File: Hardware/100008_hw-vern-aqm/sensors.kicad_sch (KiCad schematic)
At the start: 5 parts

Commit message: schematic work
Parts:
- removed C?: 10u, Capacitor_SMD:C_0805_2012Metric, symbol Device:C
- removed C?: 1u, Capacitor_SMD:C_0805_2012Metric, symbol Device:C
- removed C?: 100n, Capacitor_SMD:C_0603_1608Metric, symbol Device:C
- removed R?: 10k, Resistor_SMD:R_0603_1608Metric, symbol Device:R
- added C? (x3): 100n, Capacitor_SMD:C_0603_1608Metric, symbol Device:C
- added R? (x3): 10k, Resistor_SMD:R_0603_1608Metric, symbol Device:R
- added U?: DPS368, Components:LGA8S145X65P2X4_200X250X110-V, symbol ICs:DPS368
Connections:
- net +3V3: now also U?.19 (VDD), U?.7 (VDD), C?.1, C?.1, C?.1, R?.1, R?.1, U?.6 (VDDIO), U?.8 (VDD)
- net GND: now also U?.20 (GND), U?.21 (GND), U?.6 (GND), C?.2, C?.2, C?.2, R?.2, U?.1 (GND), U?.7 (GND)
- net I2C_SCL: now also U?.9 (SCL), R?.2, U?.4 (SCK)
- net I2C_SDA: now also U?.10 (SDA), R?.2, U?.3 (SDI)
- new net: R?.1, U?.5 (SDO)
- no-connect marks 0 -> 1
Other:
- note added: "Infineon DPS368 barometric pressure sensor"
- note added: "Sensirion SCD40 CO2 sensor"
- moved on the sheet: U?

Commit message: schematic work
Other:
- note added: "Design-in Guide SCD4x CO2 Sensor"
- note removed: "Flexible I/O worked examples"
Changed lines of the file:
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@@
 		)
 	)
-	(text_box "LAYOUT NOTE:\nEnsure good coupling to ambinet air, shield from direct sunlight and decouple from external heat sources"
+	(text_box "LAYOUT NOTE:\nEnsure good coupling to ambinet air, decouple from external heat sources, shield from direct sunlight and air turbulences"
 		(exclude_from_sim no)
-		(at 214.63 148.59 0)
-		(size 39.37 11.43)
+		(at 213.36 148.59 0)
+		(size 40.64 12.7)
 		(stroke
 			(width 0.8)
@@
 	(text_box "DESIGN NOTE:\nI2C address is 0x77 or 0x76 if SDO pin is pulled low."
 		(exclude_from_sim no)
-		(at 240.03 82.55 0)
-		(size 22.86 11.43)
+		(at 237.49 85.09 0)
+		(size 25.4 8.89)
 		(stroke
 			(width 0.8)
@@
 		)
 	)
-	(text "Flexible I/O worked examples"
+	(text "Design-in Guide SCD4x CO2 Sensor"
 		(exclude_from_sim no)
 		(at 265.43 254 0)
@@
 			)
 			(justify left bottom)
-			(href "https://jpieper.com/2022/06/30/flexible-i-o-worked-examples/")
+			(href "https://sensirion.com/media/documents/0D0C9129/623B1183/Sensirion_CO2_Sensors_SCD4x_design-in_guide.pdf")
 		)
 	)

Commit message: schematic and pcb layout
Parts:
- added C19: 100n, Capacitor_SMD:C_0603_1608Metric, symbol Device:C
- gave numbers to parts that had none: 8
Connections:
- net +3V3: now also C19.1
- net GND: now also C19.2
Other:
- moved on the sheet: C16, C17, C18, R32, R33, R34, U4, U5

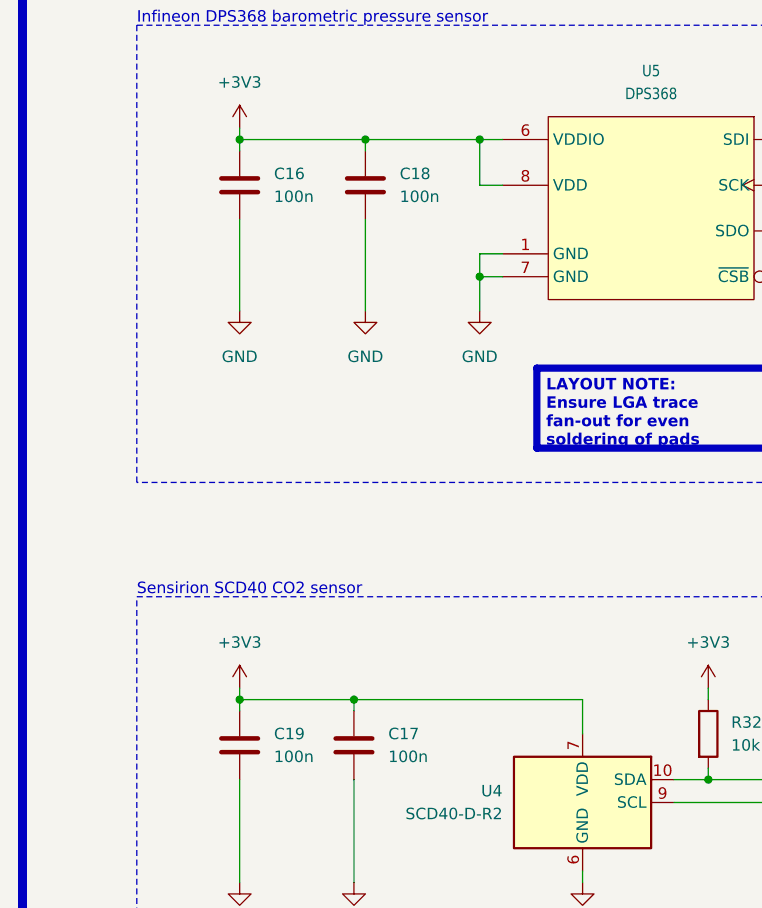
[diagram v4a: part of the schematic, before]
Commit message: schematic, pcb layout, added mouser shoping cart
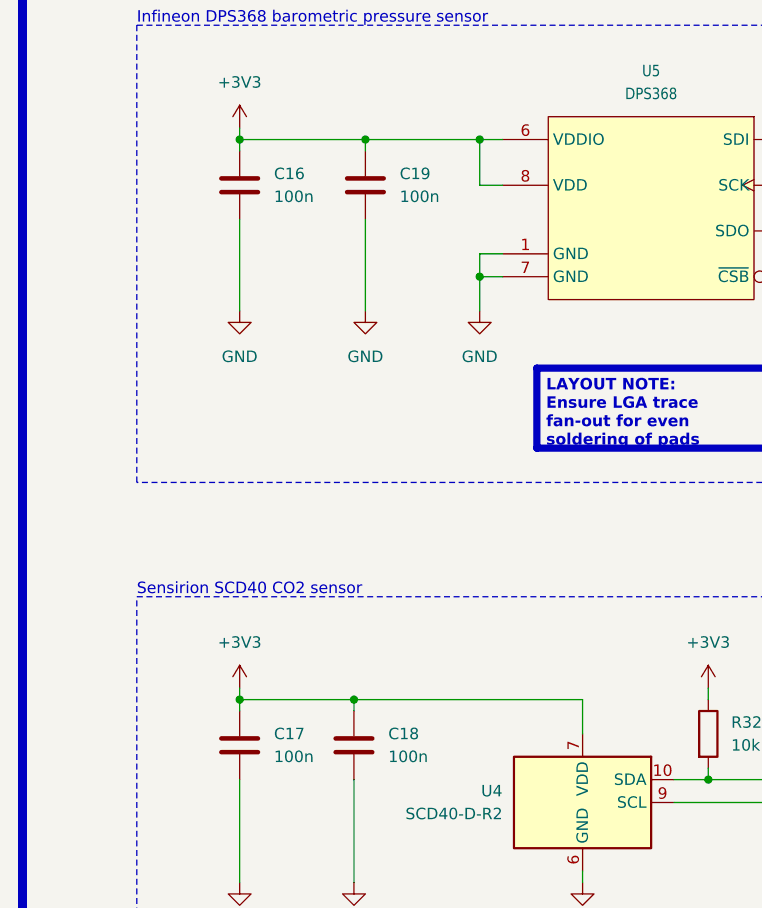
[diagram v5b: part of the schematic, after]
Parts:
- renumbered C19 to C17, C17 to C18, C18 to C19
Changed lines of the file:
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@@
 		(dnp no)
 		(fields_autoplaced yes)
-		(property "Reference" "#PWR070"
+		(property "Reference" "#PWR071"
 			(at 231.14 88.9 0)
 			(effects
@@
 		)
 		(instances
-			(project "100008_hw-vern-aqm"
-				(path "/0650c7a8-acba-429c-9f8e-eec0baf0bc1c/fede4c36-00cc-4d3d-b71c-5243ba232202/b07303a0-99ff-4a36-a427-2598198d9d06"
-					(reference "#PWR070")
+			(project ""
+				(path "/0650c7a8-acba-429c-9f8e-eec0baf0bc1c/fede4c36-00cc-4d3d-b71c-5243ba232202/b07303a0-99ff-4a36-a427-2598198d9d06"
+					(reference "#PWR0171")
 					(unit 1)
 				)
@@
 		(dnp no)
 		(fields_autoplaced yes)
-		(property "Reference" "#PWR067"
+		(property "Reference" "#PWR068"
 			(at 201.93 152.4 0)
 			(effects
@@
 		)
 		(instances
-			(project "100008_hw-vern-aqm"
-				(path "/0650c7a8-acba-429c-9f8e-eec0baf0bc1c/fede4c36-00cc-4d3d-b71c-5243ba232202/b07303a0-99ff-4a36-a427-2598198d9d06"
-					(reference "#PWR067")
+			(project ""
+				(path "/0650c7a8-acba-429c-9f8e-eec0baf0bc1c/fede4c36-00cc-4d3d-b71c-5243ba232202/b07303a0-99ff-4a36-a427-2598198d9d06"
+					(reference "#PWR0161")
 					(unit 1)
 				)
@@
 		(dnp no)
 		(fields_autoplaced yes)
-		(property "Reference" "C19"
+		(property "Reference" "C?"
 			(at 167.64 129.54 0)
 			(effects
@@
 		)
 		(instances
-			(project "100008_hw-vern-aqm"
-				(path "/0650c7a8-acba-429c-9f8e-eec0baf0bc1c/fede4c36-00cc-4d3d-b71c-5243ba232202/b07303a0-99ff-4a36-a427-2598198d9d06"
-					(reference "C19")
+			(project ""
+				(path "/0650c7a8-acba-429c-9f8e-eec0baf0bc1c/fede4c36-00cc-4d3d-b71c-5243ba232202/b07303a0-99ff-4a36-a427-2598198d9d06"
+					(reference "C17")
 					(unit 1)
 				)
@@
 		)
 		(instances
-			(project "100008_hw-vern-aqm"
-				(path "/0650c7a8-acba-429c-9f8e-eec0baf0bc1c/fede4c36-00cc-4d3d-b71c-5243ba232202/b07303a0-99ff-4a36-a427-2598198d9d06"
-					(reference "#PWR063")
+			(project ""
+				(path "/0650c7a8-acba-429c-9f8e-eec0baf0bc1c/fede4c36-00cc-4d3d-b71c-5243ba232202/b07303a0-99ff-4a36-a427-2598198d9d06"
+					(reference "#PWR0170")
 					(unit 1)
 				)
@@
 		(dnp no)
 		(fields_autoplaced yes)
-		(property "Reference" "R32"
+		(property "Reference" "R?"
 			(at 218.44 128.27 0)
 			(effects
@@
 		)
 		(instances
-			(project "100008_hw-vern-aqm"
+			(project ""
 				(path "/0650c7a8-acba-429c-9f8e-eec0baf0bc1c/fede4c36-00cc-4d3d-b71c-5243ba232202/b07303a0-99ff-4a36-a427-2598198d9d06"
 					(reference "R32")
@@
 		(dnp no)
 		(fields_autoplaced yes)
-		(property "Reference" "#PWR068"
+		(property "Reference" "#PWR069"
 			(at 215.9 128.27 0)
 			(effects
@@
 		)
 		(instances
-			(project "100008_hw-vern-aqm"
-				(path "/0650c7a8-acba-429c-9f8e-eec0baf0bc1c/fede4c36-00cc-4d3d-b71c-5243ba232202/b07303a0-99ff-4a36-a427-2598198d9d06"
-					(reference "#PWR068")
+			(project ""
+				(path "/0650c7a8-acba-429c-9f8e-eec0baf0bc1c/fede4c36-00cc-4d3d-b71c-5243ba232202/b07303a0-99ff-4a36-a427-2598198d9d06"
+					(reference "#PWR0168")
 					(unit 1)
 				)
@@
 		(dnp no)
 		(fields_autoplaced yes)
-		(property "Reference" "U5"
+		(property "Reference" "U?"
 			(at 209.55 55.88 0)
 			(effects
@@
 		)
 		(instances
-			(project "100008_hw-vern-aqm"
+			(project ""
 				(path "/0650c7a8-acba-429c-9f8e-eec0baf0bc1c/fede4c36-00cc-4d3d-b71c-5243ba232202/b07303a0-99ff-4a36-a427-2598198d9d06"
 					(reference "U5")
@@
 		(dnp no)
 		(fields_autoplaced yes)
-		(property "Reference" "#PWR065"
+		(property "Reference" "#PWR066"
 			(at 177.8 88.9 0)
 			(effects
@@
 		)
 		(instances
-			(project "100008_hw-vern-aqm"
-				(path "/0650c7a8-acba-429c-9f8e-eec0baf0bc1c/fede4c36-00cc-4d3d-b71c-5243ba232202/b07303a0-99ff-4a36-a427-2598198d9d06"
-					(reference "#PWR065")
+			(project ""
+				(path "/0650c7a8-acba-429c-9f8e-eec0baf0bc1c/fede4c36-00cc-4d3d-b71c-5243ba232202/b07303a0-99ff-4a36-a427-2598198d9d06"
+					(reference "#PWR0165")
 					(unit 1)
 				)
@@
 		(dnp yes)
 		(fields_autoplaced yes)
-		(property "Reference" "R34"
+		(property "Reference" "R?"
 			(at 233.68 76.2 0)
 			(effects
@@
 		)
 		(instances
-			(project "100008_hw-vern-aqm"
+			(project ""
 				(path "/0650c7a8-acba-429c-9f8e-eec0baf0bc1c/fede4c36-00cc-4d3d-b71c-5243ba232202/b07303a0-99ff-4a36-a427-2598198d9d06"
 					(reference "R34")
@@
 		(dnp no)
 		(fields_autoplaced yes)
-		(property "Reference" "U4"
+		(property "Reference" "U?"
 			(at 193.04 135.8899 0)
 			(effects
@@
 		)
 		(instances
-			(project "100008_hw-vern-aqm"
+			(project ""
 				(path "/0650c7a8-acba-429c-9f8e-eec0baf0bc1c/fede4c36-00cc-4d3d-b71c-5243ba232202/b07303a0-99ff-4a36-a427-2598198d9d06"
 					(reference "U4")
@@
 		)
 		(instances
-			(project "100008_hw-vern-aqm"
-				(path "/0650c7a8-acba-429c-9f8e-eec0baf0bc1c/fede4c36-00cc-4d3d-b71c-5243ba232202/b07303a0-99ff-4a36-a427-2598198d9d06"
-					(reference "#PWR061")
+			(project ""
+				(path "/0650c7a8-acba-429c-9f8e-eec0baf0bc1c/fede4c36-00cc-4d3d-b71c-5243ba232202/b07303a0-99ff-4a36-a427-2598198d9d06"
+					(reference "#PWR0164")
 					(unit 1)
 				)
@@
 		)
 		(instances
-			(project "100008_hw-vern-aqm"
-				(path "/0650c7a8-acba-429c-9f8e-eec0baf0bc1c/fede4c36-00cc-4d3d-b71c-5243ba232202/b07303a0-99ff-4a36-a427-2598198d9d06"
-					(reference "#PWR062")
+			(project ""
+				(path "/0650c7a8-acba-429c-9f8e-eec0baf0bc1c/fede4c36-00cc-4d3d-b71c-5243ba232202/b07303a0-99ff-4a36-a427-2598198d9d06"
+					(reference "#PWR0166")
 					(unit 1)
 				)
@@
 		(dnp no)
 		(fields_autoplaced yes)
-		(property "Reference" "R33"
+		(property "Reference" "R?"
 			(at 227.33 128.27 0)
 			(effects
@@
 		)
 		(instances
-			(project "100008_hw-vern-aqm"
+			(project ""
 				(path "/0650c7a8-acba-429c-9f8e-eec0baf0bc1c/fede4c36-00cc-4d3d-b71c-5243ba232202/b07303a0-99ff-4a36-a427-2598198d9d06"
 					(reference "R33")
@@
 		(dnp no)
 		(fields_autoplaced yes)
-		(property "Reference" "#PWR066"
+		(property "Reference" "#PWR067"
 			(at 190.5 88.9 0)
 			(effects
@@
 		)
 		(instances
-			(project "100008_hw-vern-aqm"
-				(path "/0650c7a8-acba-429c-9f8e-eec0baf0bc1c/fede4c36-00cc-4d3d-b71c-5243ba232202/b07303a0-99ff-4a36-a427-2598198d9d06"
-					(reference "#PWR066")
+			(project ""
+				(path "/0650c7a8-acba-429c-9f8e-eec0baf0bc1c/fede4c36-00cc-4d3d-b71c-5243ba232202/b07303a0-99ff-4a36-a427-2598198d9d06"
+					(reference "#PWR0163")
 					(unit 1)
 				)
@@
 		(dnp no)
 		(fields_autoplaced yes)
-		(property "Reference" "#PWR064"
+		(property "Reference" "#PWR065"
 			(at 176.53 152.4 0)
 			(effects
@@
 		)
 		(instances
-			(project "100008_hw-vern-aqm"
-				(path "/0650c7a8-acba-429c-9f8e-eec0baf0bc1c/fede4c36-00cc-4d3d-b71c-5243ba232202/b07303a0-99ff-4a36-a427-2598198d9d06"
-					(reference "#PWR064")
+			(project ""
+				(path "/0650c7a8-acba-429c-9f8e-eec0baf0bc1c/fede4c36-00cc-4d3d-b71c-5243ba232202/b07303a0-99ff-4a36-a427-2598198d9d06"
+					(reference "#PWR0169")
 					(unit 1)
 				)
@@
 		(dnp no)
 		(fields_autoplaced yes)
-		(property "Reference" "C16"
+		(property "Reference" "C?"
 			(at 167.64 67.31 0)
 			(effects
@@
 		)
 		(instances
-			(project "100008_hw-vern-aqm"
+			(project ""
 				(path "/0650c7a8-acba-429c-9f8e-eec0baf0bc1c/fede4c36-00cc-4d3d-b71c-5243ba232202/b07303a0-99ff-4a36-a427-2598198d9d06"
 					(reference "C16")
@@
 		(dnp no)
 		(fields_autoplaced yes)
-		(property "Reference" "#PWR071"
+		(property "Reference" "#PWR064"
 			(at 163.83 152.4 0)
 			(effects
@@
 		)
 		(instances
-			(project "100008_hw-vern-aqm"
-				(path "/0650c7a8-acba-429c-9f8e-eec0baf0bc1c/fede4c36-00cc-4d3d-b71c-5243ba232202/b07303a0-99ff-4a36-a427-2598198d9d06"
-					(reference "#PWR071")
+			(project ""
+				(path "/0650c7a8-acba-429c-9f8e-eec0baf0bc1c/fede4c36-00cc-4d3d-b71c-5243ba232202/b07303a0-99ff-4a36-a427-2598198d9d06"
+					(reference "#PWR0162")
 					(unit 1)
 				)
@@
 		(dnp no)
 		(fields_autoplaced yes)
-		(property "Reference" "C17"
+		(property "Reference" "C?"
 			(at 180.34 129.54 0)
 			(effects
@@
 		)
 		(instances
-			(project "100008_hw-vern-aqm"
-				(path "/0650c7a8-acba-429c-9f8e-eec0baf0bc1c/fede4c36-00cc-4d3d-b71c-5243ba232202/b07303a0-99ff-4a36-a427-2598198d9d06"
-					(reference "C17")
+			(project ""
+				(path "/0650c7a8-acba-429c-9f8e-eec0baf0bc1c/fede4c36-00cc-4d3d-b71c-5243ba232202/b07303a0-99ff-4a36-a427-2598198d9d06"
+					(reference "C18")
 					(unit 1)
 				)
@@
 		(dnp no)
 		(fields_autoplaced yes)
-		(property "Reference" "C18"
+		(property "Reference" "C?"
 			(at 181.61 67.31 0)
 			(effects
@@
 		)
 		(instances
-			(project "100008_hw-vern-aqm"
-				(path "/0650c7a8-acba-429c-9f8e-eec0baf0bc1c/fede4c36-00cc-4d3d-b71c-5243ba232202/b07303a0-99ff-4a36-a427-2598198d9d06"
-					(reference "C18")
+			(project ""
+				(path "/0650c7a8-acba-429c-9f8e-eec0baf0bc1c/fede4c36-00cc-4d3d-b71c-5243ba232202/b07303a0-99ff-4a36-a427-2598198d9d06"
+					(reference "C19")
 					(unit 1)
 				)
@@
 		(dnp no)
 		(fields_autoplaced yes)
-		(property "Reference" "#PWR069"
+		(property "Reference" "#PWR070"
 			(at 224.79 128.27 0)
 			(effects
@@
 		)
 		(instances
-			(project "100008_hw-vern-aqm"
-				(path "/0650c7a8-acba-429c-9f8e-eec0baf0bc1c/fede4c36-00cc-4d3d-b71c-5243ba232202/b07303a0-99ff-4a36-a427-2598198d9d06"
-					(reference "#PWR069")
-					(unit 1)
-				)
+			(project ""
+				(path "/0650c7a8-acba-429c-9f8e-eec0baf0bc1c/fede4c36-00cc-4d3d-b71c-5243ba232202/b07303a0-99ff-4a36-a427-2598198d9d06"
+					(reference "#PWR0167")
+					(unit 1)
+				)
